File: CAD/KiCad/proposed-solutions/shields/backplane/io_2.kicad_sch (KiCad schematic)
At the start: 11 parts

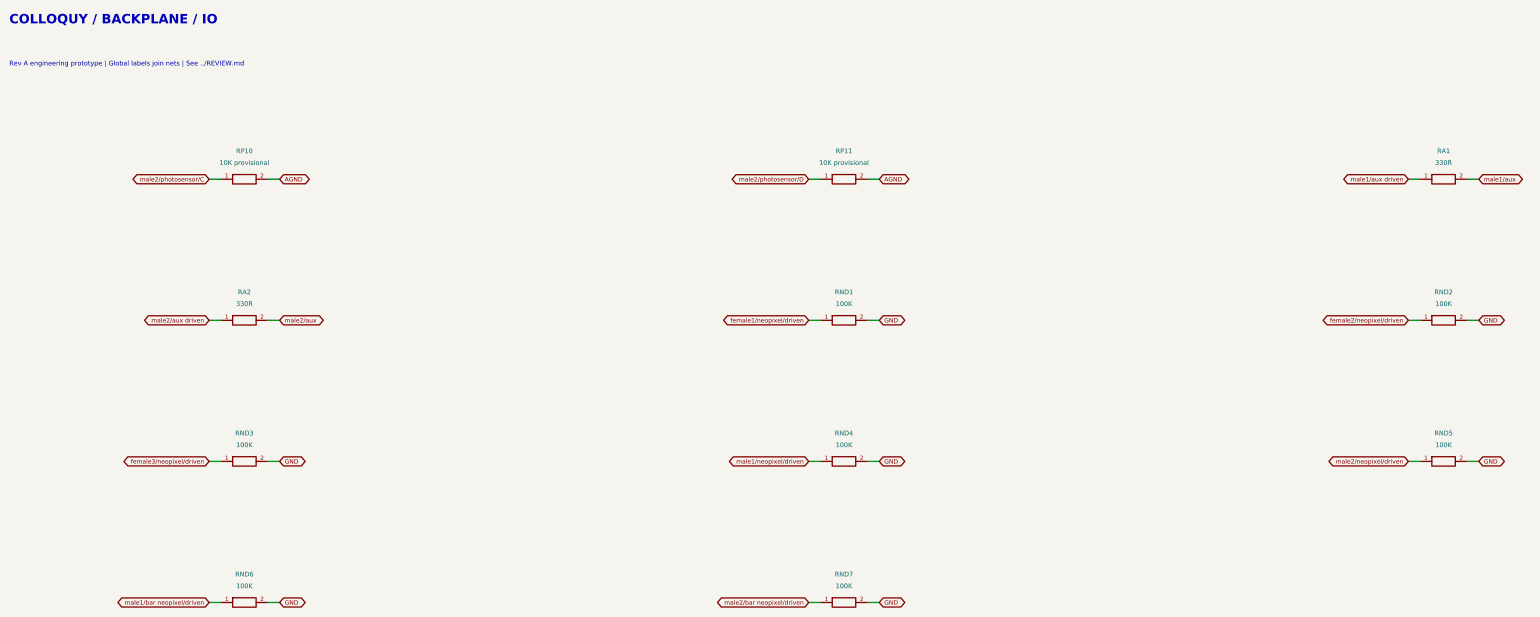
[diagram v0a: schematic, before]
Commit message: Size RA1/RA2 for the males' state lamps: 160R
The aux lines end on TJ's backlight panels, and RA is all that sets
their current. 330R gave about 5.5 mA, half the panel's recommended
least; 160R gives 11 mA nominal and stays under the SN74LV4T125's
16 mA at every corner, so the Mega and the Teensy can both drive them.

Packages, reports, wired drawing and pinouts regenerated; the pinout
generator now reads each series value from the backplane circuit.

Co-Authored-By: Claude Opus 5.5 <noreply@anthropic.com>
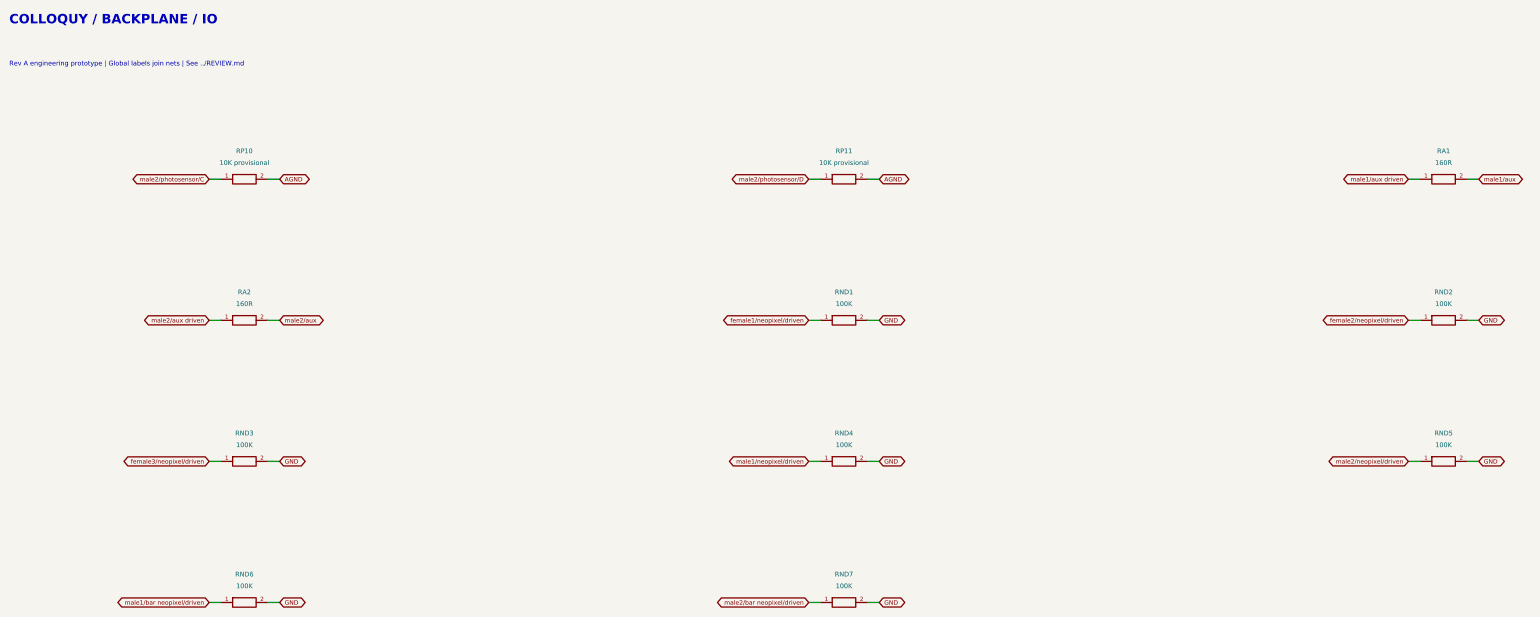
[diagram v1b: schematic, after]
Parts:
- RA1, RA2: value 330R -> 160R
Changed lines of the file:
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@@
 (symbol (lib_id "Colloquy:RA1") (at 325.1200 50.8000 0) (unit 1) (exclude_from_sim no) (in_bom yes) (on_board yes) (dnp no)
 (property "Reference" "RA1" (at 325.1200 44.7040 0) (effects (font (size 1.016 1.016))  ))
-(property "Value" "330R" (at 325.1200 47.2440 0) (effects (font (size 1.016 1.016))  ))
+(property "Value" "160R" (at 325.1200 47.2440 0) (effects (font (size 1.016 1.016))  ))
 (property "Footprint" "Shields:R_0603_1608Metric" (at 325.1200 50.8000 0) (effects (font (size 1.27 1.27))  (hide yes)))
 (property "Datasheet" "" (at 325.1200 50.8000 0) (effects (font (size 1.27 1.27))  (hide yes)))
@@
 (symbol (lib_id "Colloquy:RA2") (at 66.0400 81.2800 0) (unit 1) (exclude_from_sim no) (in_bom yes) (on_board yes) (dnp no)
 (property "Reference" "RA2" (at 66.0400 75.1840 0) (effects (font (size 1.016 1.016))  ))
-(property "Value" "330R" (at 66.0400 77.7240 0) (effects (font (size 1.016 1.016))  ))
+(property "Value" "160R" (at 66.0400 77.7240 0) (effects (font (size 1.016 1.016))  ))
 (property "Footprint" "Shields:R_0603_1608Metric" (at 66.0400 81.2800 0) (effects (font (size 1.27 1.27))  (hide yes)))
 (property "Datasheet" "" (at 66.0400 81.2800 0) (effects (font (size 1.27 1.27))  (hide yes)))
